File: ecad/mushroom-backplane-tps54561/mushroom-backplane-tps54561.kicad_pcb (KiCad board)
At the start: 2 copper layers, 24 x 63 mm, 43 parts, among them J1 BUSOUT, J2 BUSIN, J3 BACKPLANE, M1 KK 254, Q1 AO3400A, Q2 SI2301CDS-T1-GE3, U1 TPS54561

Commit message: Organize ECAD files
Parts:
- U1: footprint Mycelium:WSON-10-1EP_4x4mm_P0.8_EP2.6x3.0mm -> mykilio:WSON-10-1EP_4x4mm_P0.8_EP2.6x3.0mm
- moved C13 2.93 mm to (89.7, 96.8), turned to 90 degrees
- moved C9 2.48 mm to (102.8, 94.4), turned to 90 degrees
- moved R7 1.79 mm to (100.8, 95.2), turned to 180 degrees
- moved C15 0.99 mm to (93.8, 96.9), turned to 90 degrees
- moved R8 0.72 mm to (99.8, 93.6)
- moved C14 0.11 mm to (95.4, 112.7)
- moved C16 0.11 mm to (93.0, 112.7)
- moved C17 0.11 mm to (90.6, 112.7)
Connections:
- U1 pad 4: Net-(R7-Pad1) -> Net-(C9-Pad1)
- U1 pad 5: Net-(C9-Pad1) -> Net-(R7-Pad1)
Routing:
- net Net-(C9-Pad1): track 1.28 -> 3.76 mm
- net Net-(R7-Pad1): track 2.67 -> 1.65 mm
- net Net-(C13-Pad1): track 2.31 -> 1.32 mm
- net 5VSMPS: track 53.5 -> 54.0 mm

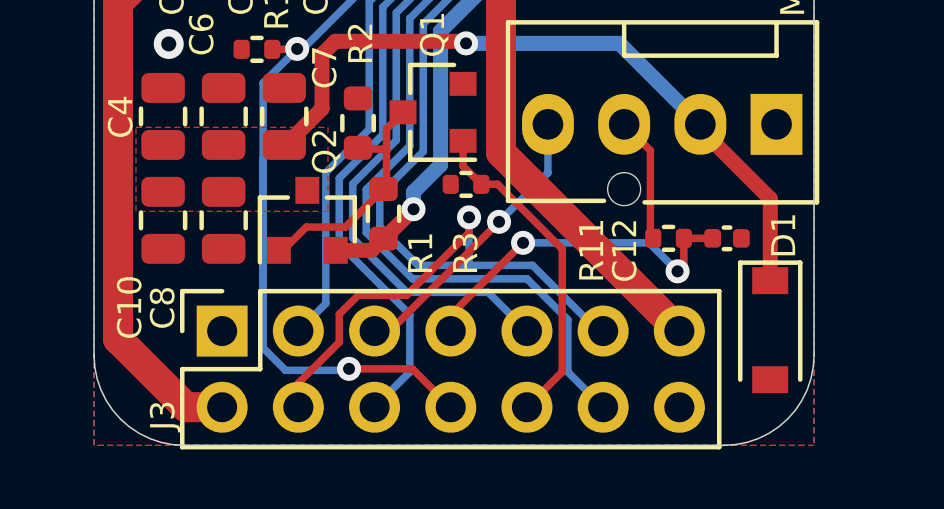
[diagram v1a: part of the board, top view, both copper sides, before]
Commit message: Align pin numbering of backplane and blade
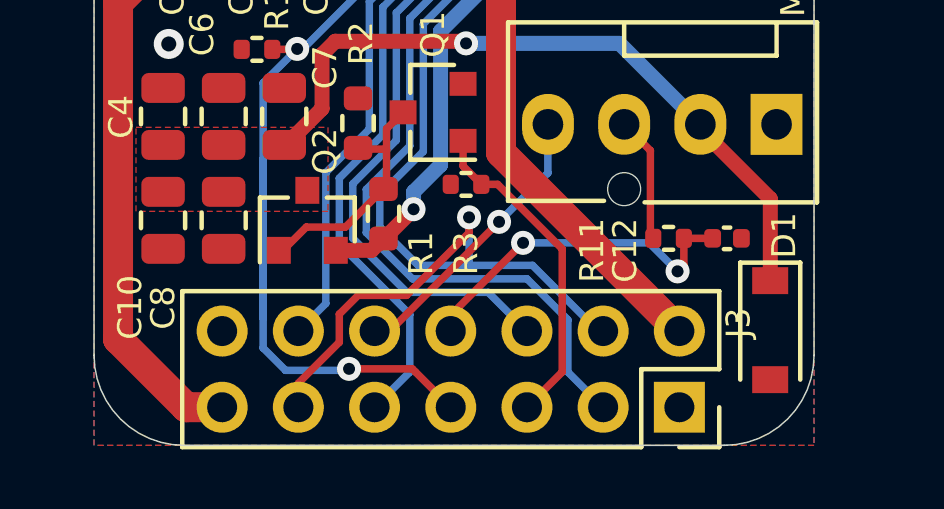
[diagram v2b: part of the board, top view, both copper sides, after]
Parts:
- moved J3 15.5 mm to (107.5, 130.2), turned to 270 degrees
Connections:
- J3 pad 10: FANDCC -> FANPWM
- J3 pad 12: SCL -> SDA
- J3 pad 3: SDA -> SCL
- J3 pad 5: FANPWM -> FANDCC
- J3 pad 6: STX -> SRX
- J3 pad 7: FANFDB -> POWTMP
- J3 pad 8: POWTMP -> FANFDB
- J3 pad 9: SRX -> STX
